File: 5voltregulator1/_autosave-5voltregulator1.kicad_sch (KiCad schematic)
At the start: 5 parts, among them U1 L7805

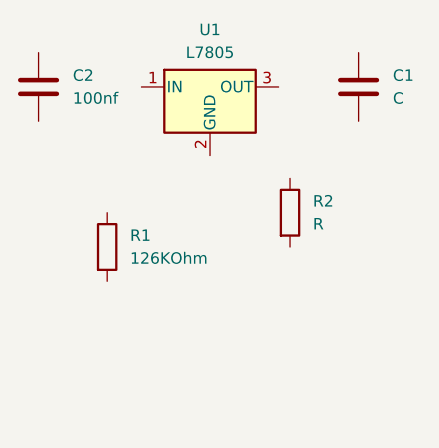
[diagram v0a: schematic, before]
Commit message: Made custom ic symbol and started 3d model
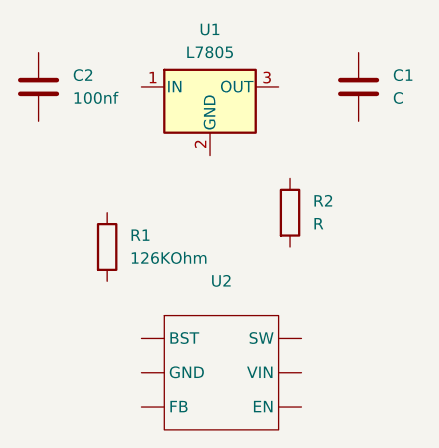
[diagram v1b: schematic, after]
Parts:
- added U2: ~, symbol TP6841S6:TP6841S6
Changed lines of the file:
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@@
+	)
+	(symbol
+		(lib_id "TP6841S6:TP6841S6")
+		(at 135.89 123.19 0)
+		(unit 1)
+		(exclude_from_sim no)
+		(in_bom yes)
+		(on_board yes)
+		(dnp no)
+		(fields_autoplaced yes)
+		(property "Reference" "U2"
+			(at 135.89 114.3 0)
+			(effects
+				(font
+					(size 1.27 1.27)
+				)
+			)
+		)
+		(property "Value" "~"
+			(at 135.89 116.84 0)
+			(effects
+				(font
+					(size 1.27 1.27)
+				)
+			)
+		)
+		(property "Footprint" ""
+			(at 135.89 123.19 0)
+			(effects
+				(font
+					(size 1.27 1.27)
+				)
+				(hide yes)
+			)
+		)
+		(property "Datasheet" ""
+			(at 135.89 123.19 0)
+			(effects
+				(font
+					(size 1.27 1.27)
+				)
+				(hide yes)
+			)
+		)
+		(property "Description" ""
+			(at 135.89 123.19 0)
+			(effects
+				(font
+					(size 1.27 1.27)
+				)
+				(hide yes)
+			)
+		)
+		(pin ""
+		)
+		(pin ""
+		)
+		(pin ""
+		)
+		(pin ""
+		)
+		(pin ""
+		)
+		(pin ""
+		)
+		(instances
+			(project ""
+				(path "/e8d32d05-777d-4b25-b169-58c56f6de1e5"
+					(reference "U2")
+					(unit 1)
+				)
+			)
+		)
 	)
 	(symbol
